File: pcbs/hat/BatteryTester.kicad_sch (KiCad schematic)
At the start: 1 part, among them J1 Screw_Terminal_01x02

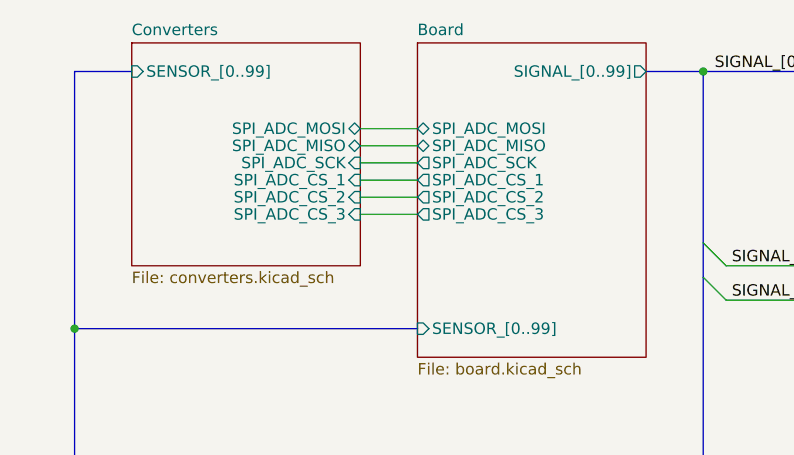
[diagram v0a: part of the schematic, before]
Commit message: change ADCs and connect all Sensors and Signals
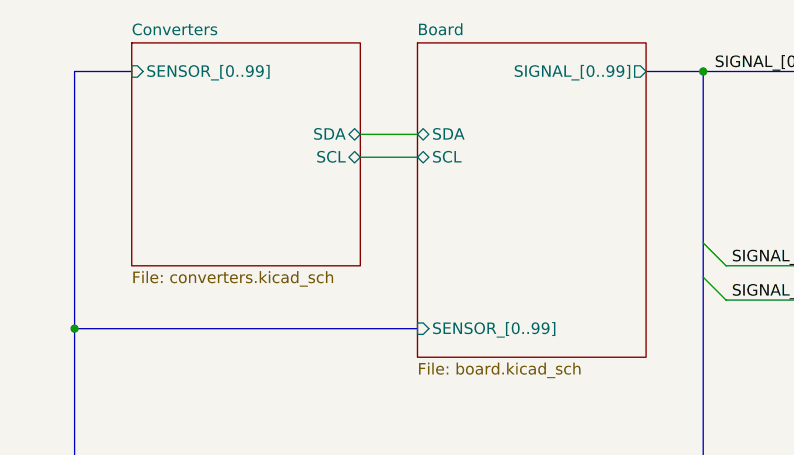
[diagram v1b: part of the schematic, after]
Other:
- sheet Board ports: added SCL, SDA; removed SPI_ADC_CS_1, SPI_ADC_CS_2, SPI_ADC_CS_3, SPI_ADC_MISO, SPI_ADC_MOSI, SPI_ADC_SCK
- sheet Converters ports: added SCL, SDA; removed SPI_ADC_CS_1, SPI_ADC_CS_2, SPI_ADC_CS_3, SPI_ADC_MISO, SPI_ADC_MOSI, SPI_ADC_SCK

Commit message: formatting
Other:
- note added: "Power Supply Connector"
- moved on the sheet: J1
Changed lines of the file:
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@@
   (junction (at 165.1 146.05) (diameter 0) (color 0 0 0 0)
   )
-  (junction (at 31.75 53.975) (diameter 0) (color 0 0 0 0)
+  (junction (at 31.75 47.625) (diameter 0) (color 0 0 0 0)
   )
   (bus_entry (at 238.76 127) (size 2.54 2.54)
@@
     (stroke (width 0) (type default) (color 0 0 0 0))
   )
-  (bus (pts (xy 31.75 53.975) (xy 31.75 146.05))
-    (stroke (width 0) (type default) (color 0 0 0 0))
-  )
   (wire (pts (xy 222.25 134.62) (xy 238.76 134.62))
     (stroke (width 0) (type default) (color 0 0 0 0))
@@
     (stroke (width 0) (type default) (color 0 0 0 0))
   )
+  (polyline (pts (xy 12.7 196.85) (xy 69.85 196.85))
+    (stroke (width 0) (type default) (color 0 0 0 0))
+  )
   (bus (pts (xy 165.1 74.93) (xy 165.1 78.74))
     (stroke (width 0) (type default) (color 0 0 0 0))
@@
     (stroke (width 0) (type default) (color 0 0 0 0))
   )
-  (bus (pts (xy 31.75 53.975) (xy 69.85 53.975))
-    (stroke (width 0) (type default) (color 0 0 0 0))
-  )
   (bus (pts (xy 241.3 49.53) (xy 241.3 53.34))
     (stroke (width 0) (type default) (color 0 0 0 0))
@@
     (stroke (width 0) (type default) (color 0 0 0 0))
   )
-  (wire (pts (xy 50.8 184.785) (xy 43.18 184.785))
+  (wire (pts (xy 46.99 189.23) (xy 39.37 189.23))
     (stroke (width 0) (type default) (color 0 0 0 0))
   )
@@
     (stroke (width 0) (type default) (color 0 0 0 0))
   )
+  (polyline (pts (xy 69.85 196.85) (xy 69.85 155.575))
+    (stroke (width 0) (type default) (color 0 0 0 0))
+  )
   (wire (pts (xy 222.25 109.22) (xy 238.76 109.22))
     (stroke (width 0) (type default) (color 0 0 0 0))
@@
     (stroke (width 0) (type default) (color 0 0 0 0))
   )
+  (bus (pts (xy 31.75 47.625) (xy 31.75 146.05))
+    (stroke (width 0) (type default) (color 0 0 0 0))
+  )
   (bus (pts (xy 241.3 111.76) (xy 241.3 125.73))
     (stroke (width 0) (type default) (color 0 0 0 0))
   )
+  (polyline (pts (xy 12.7 155.575) (xy 12.7 196.85))
+    (stroke (width 0) (type default) (color 0 0 0 0))
+  )
   (wire (pts (xy 146.05 80.01) (xy 162.56 80.01))
     (stroke (width 0) (type default) (color 0 0 0 0))
@@
     (stroke (width 0) (type default) (color 0 0 0 0))
   )
+  (polyline (pts (xy 12.7 155.575) (xy 69.85 155.575))
+    (stroke (width 0) (type default) (color 0 0 0 0))
+  )
   (bus (pts (xy 165.1 53.34) (xy 165.1 57.15))
     (stroke (width 0) (type default) (color 0 0 0 0))
@@
     (stroke (width 0) (type default) (color 0 0 0 0))
   )
-  (wire (pts (xy 43.18 182.245) (xy 50.8 182.245))
+  (wire (pts (xy 39.37 186.69) (xy 46.99 186.69))
     (stroke (width 0) (type default) (color 0 0 0 0))
   )
@@
     (stroke (width 0) (type default) (color 0 0 0 0))
   )
+  (bus (pts (xy 69.85 47.625) (xy 31.75 47.625))
+    (stroke (width 0) (type default) (color 0 0 0 0))
+  )
   (wire (pts (xy 180.34 46.99) (xy 196.85 46.99))
     (stroke (width 0) (type default) (color 0 0 0 0))
@@
     (stroke (width 0) (type default) (color 0 0 0 0))
   )
+  (bus (pts (xy 31.75 25.4) (xy 31.75 47.625))
+    (stroke (width 0) (type default) (color 0 0 0 0))
+  )
   (wire (pts (xy 104.14 127) (xy 120.65 127))
     (stroke (width 0) (type default) (color 0 0 0 0))
@@
     (stroke (width 0) (type default) (color 0 0 0 0))
   )
-  (bus (pts (xy 31.75 25.4) (xy 31.75 53.975))
-    (stroke (width 0) (type default) (color 0 0 0 0))
-  )
   (bus (pts (xy 101.6 48.26) (xy 101.6 69.85))
     (stroke (width 0) (type default) (color 0 0 0 0))
@@
     (stroke (width 0) (type default) (color 0 0 0 0))
   )
-  (text "SUPPLY 8-9V" (at 48.26 174.625 180)
+  (text "Power Supply\n  Connector" (at 21.59 171.45 0)
+    (effects (font (size 3.81 3.81)) (justify left bottom))
+  )
+  (text "SUPPLY 8-9V" (at 44.45 179.07 180)
     (effects (font (size 1.27 1.27)) (justify right bottom))
   )
@@
     (effects (font (size 1.27 1.27)) (justify right bottom))
   )
-  (symbol (lib_id "power:GND") (at 50.8 184.785 90) (unit 1)
+  (symbol (lib_id "power:GND") (at 46.99 189.23 90) (unit 1)
     (in_bom yes) (on_board yes) (fields_autoplaced)
-    (property "Reference" "#PWR02" (id 0) (at 57.15 184.785 0)
+    (property "Reference" "#PWR02" (id 0) (at 53.34 189.23 0)
       (effects (font (size 1.27 1.27)) hide)
     )
-    (property "Value" "GND" (id 1) (at 54.61 184.7849 90)
+    (property "Value" "GND" (id 1) (at 50.8 189.2299 90)
       (effects (font (size 1.27 1.27)) (justify right))
     )
-    (property "Footprint" "" (id 2) (at 50.8 184.785 0)
+    (property "Footprint" "" (id 2) (at 46.99 189.23 0)
       (effects (font (size 1.27 1.27)) hide)
     )
-    (property "Datasheet" "" (id 3) (at 50.8 184.785 0)
+    (property "Datasheet" "" (id 3) (at 46.99 189.23 0)
       (effects (font (size 1.27 1.27)) hide)
     )
     (pin "1")
   )
-  (symbol (lib_id "power:VCC") (at 50.8 182.245 270) (unit 1)
+  (symbol (lib_id "power:VCC") (at 46.99 186.69 270) (unit 1)
     (in_bom yes) (on_board yes) (fields_autoplaced)
-    (property "Reference" "#PWR01" (id 0) (at 46.99 182.245 0)
+    (property "Reference" "#PWR01" (id 0) (at 43.18 186.69 0)
       (effects (font (size 1.27 1.27)) hide)
     )
-    (property "Value" "VCC" (id 1) (at 54.61 182.2449 90)
+    (property "Value" "VCC" (id 1) (at 50.8 186.6899 90)
       (effects (font (size 1.27 1.27)) (justify left))
     )
-    (property "Footprint" "" (id 2) (at 50.8 182.245 0)
+    (property "Footprint" "" (id 2) (at 46.99 186.69 0)
       (effects (font (size 1.27 1.27)) hide)
     )
-    (property "Datasheet" "" (id 3) (at 50.8 182.245 0)
+    (property "Datasheet" "" (id 3) (at 46.99 186.69 0)
       (effects (font (size 1.27 1.27)) hide)
     )
     (pin "1")
   )
-  (symbol (lib_id "Connector:Screw_Terminal_01x02") (at 38.1 182.245 0) (mirror y) (unit 1)
+  (symbol (lib_id "Connector:Screw_Terminal_01x02") (at 34.29 186.69 0) (mirror y) (unit 1)
     (in_bom yes) (on_board yes) (fields_autoplaced)
-    (property "Reference" "J1" (id 0) (at 38.1 175.895 0))
-    (property "Value" "Screw_Terminal_01x02" (id 1) (at 38.1 178.435 0))
-    (property "Footprint" "TerminalBlock:TerminalBlock_bornier-2_P5.08mm" (id 2) (at 38.1 182.245 0)
+    (property "Reference" "J1" (id 0) (at 34.29 180.34 0))
+    (property "Value" "Screw_Terminal_01x02" (id 1) (at 34.29 182.88 0))
+    (property "Footprint" "TerminalBlock:TerminalBlock_bornier-2_P5.08mm" (id 2) (at 34.29 186.69 0)
       (effects (font (size 1.27 1.27)) hide)
     )
-    (property "Datasheet" "~" (id 3) (at 38.1 182.245 0)
+    (property "Datasheet" "~" (id 3) (at 34.29 186.69 0)
       (effects (font (size 1.27 1.27)) hide)
     )
@@
     )
   )
-  (sheet (at 69.85 22.225) (size 25.4 34.925) (fields_autoplaced)
+  (sheet (at 69.85 22.225) (size 25.4 28.575) (fields_autoplaced)
     (stroke (width 0.1524) (type solid) (color 0 0 0 0))
     (fill (color 0 0 0 0.0000))
@@
       (effects (font (size 1.27 1.27)) (justify left bottom))
     )
-    (property "Sheet file" "board.kicad_sch" (id 1) (at 69.85 57.7346 0)
+    (property "Sheet file" "board.kicad_sch" (id 1) (at 69.85 51.3846 0)
       (effects (font (size 1.27 1.27)) (justify left top))
     )
@@
       (effects (font (size 1.27 1.27)) (justify right))
     )
-    (pin "SENSOR_[0..99]" input (at 69.85 53.975 180)
+    (pin "SENSOR_[0..99]" input (at 69.85 47.625 180)
       (effects (font (size 1.27 1.27)) (justify left))
     )
@@
     )
   )
-  (sheet (at 38.1 22.225) (size 25.4 24.765) (fields_autoplaced)
+  (sheet (at 38.1 22.225) (size 25.4 18.415) (fields_autoplaced)
     (stroke (width 0.1524) (type solid) (color 0 0 0 0))
     (fill (color 0 0 0 0.0000))
@@
       (effects (font (size 1.27 1.27)) (justify left bottom))
     )
-    (property "Sheet file" "converters.kicad_sch" (id 1) (at 38.1 47.5746 0)
+    (property "Sheet file" "converters.kicad_sch" (id 1) (at 38.1 41.2246 0)
       (effects (font (size 1.27 1.27)) (justify left top))
     )

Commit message: few little change
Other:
- note added: "SUPPLY 7-9V (2S LiPo)"
- note removed: "SUPPLY 8-9V"

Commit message: add memory + check footprints
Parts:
- J1: value Screw_Terminal_01x02 -> Supply Connector; footprint TerminalBlock:TerminalBlock_bornier-2_P5.08mm -> Connector_Phoenix_MSTB:PhoenixContact_MSTBA_2,5_2-G-5,08_1x02_P5.08mm_Horizontal
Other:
- sheet Board ports: added ADC_SCL, ADC_SDA, MEM_MISO, MEM_MOSI, MEM_SCK, ~{MEM_CE}; removed SCL, SDA
- sheet Converters ports: added ADC_SCL, ADC_SDA, MEM_MISO, MEM_MOSI, MEM_SCK, ~{MEM_CE}; removed SCL, SDA
